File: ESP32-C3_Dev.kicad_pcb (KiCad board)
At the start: 2 copper layers, 30.7 x 37.2 mm, 58 parts, among them J1 Conn_01x09_Pin, J2 Conn_01x02_Pin, J3 Conn_01x09_Pin, J4 USB_C_Receptacle_USB2.0_16P, J5 Conn_01x03_Socket, J6 Conn_01x03_Socket, J7 Conn_01x04_Pin, SW1 SW_MEC_5G, SW2 SW_MEC_5G, U1 ESP32-C3-WROOM-02, U2 AMS1117-3.3, U3 MCP73831-2-OT, U4 TLV9002S, U5 OLED_SSD1306

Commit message: wip schematic
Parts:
- removed D7: 1N5819WS, Diode_SMD:D_SOD-323
- removed J2: Conn_01x02_Pin, TerminalBlock_Phoenix:TerminalBlock_Phoenix_MKDS-1-2-3.81_1x02_P3.81mm_Horizontal
- removed J3: Conn_01x09_Pin, Connector_PinHeader_2.54mm:PinHeader_1x09_P2.54mm_Vertical
- added C13: 4u7, Capacitor_SMD:C_0603_1608Metric, F.Cu at (190.3, 99.5)
- added D8: 1N5819WS, Diode_SMD:D_SOD-323, F.Cu at (202.9, 114.0)
- added J8: Conn_01x02_Pin, TerminalBlock_Phoenix:TerminalBlock_Phoenix_MKDS-1-2-3.81_1x02_P3.81mm_Horizontal, F.Cu at (195.3, 103.0)
- added Q1: Dual_NMOS_8205A, Package_TO_SOT_SMD:SOT-23-6, F.Cu at (203.4, 110.3)
- added R16: 10K, Resistor_SMD:R_0603_1608Metric, F.Cu at (190.3, 102.1)
- added R18: 10K, Resistor_SMD:R_0603_1608Metric, F.Cu at (190.3, 104.6)
- added R19: 10K, Resistor_SMD:R_0603_1608Metric, F.Cu at (190.3, 107.1)
- added R20: 100K, Resistor_SMD:R_0603_1608Metric, F.Cu at (190.3, 109.6)
- added R21: 100K, Resistor_SMD:R_0603_1608Metric, F.Cu at (190.3, 112.1)
- added R22: 10k, Resistor_SMD:R_0603_1608Metric, F.Cu at (209.9, 99.5)
- added R23: 10k, Resistor_SMD:R_0603_1608Metric, F.Cu at (209.9, 102.1)
- added U6: TP4056, Package_SO:SOIC-8-1EP_3.9x4.9mm_P1.27mm_EP2.41x3.3mm_ThermalVias, F.Cu at (196.6, 111.3)
- C6, C9: value 4u7 -> 100n
- D5: value LED -> LED Rot
- D6: value LED -> LED Blau
- R7: value 10K -> 100R
- R8: value 10K -> 1K
- U3: value MCP73831-2-OT -> DW01A; footprint Package_TO_SOT_SMD:SOT-23-5 -> Package_TO_SOT_SMD:SOT-23-6
- moved C10 8.80 mm to (179.8, 70.4)
- moved C11 8.80 mm to (179.8, 72.9)
- moved C12 8.80 mm to (179.8, 75.4)
- moved R10 8.80 mm to (179.8, 80.4)
- moved R11 8.80 mm to (179.8, 82.9)
- moved R12 8.80 mm to (183.8, 70.4)
- moved R13 8.80 mm to (183.8, 72.9)
- moved R14 8.80 mm to (183.8, 75.4)
- moved R15 8.80 mm to (183.8, 77.9)
- moved R17 8.80 mm to (183.8, 80.4)
- moved R9 8.80 mm to (179.8, 77.9)
- moved U4 8.80 mm to (181.5, 86.5)
- moved J1 7.36 mm to (118.5, 68.7)
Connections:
- C6 pad 1: +5V -> USB5V
- C9 pad 1: /Power Supply/battery+ -> Net-(U3-VCC)
- C9 pad 2: GND -> /Power Supply/battery-
- D2 pad 2: /Power Supply/USB5V -> USB5V
- D4 pad 1: /Power Supply/USB5V -> USB5V
- J1 pad 1: /Controller/GPIO4 -> unconnected-(J1-Pin_1-Pad1)
- J1 pad 2: /Controller/GPIO5 -> unconnected-(J1-Pin_2-Pad2)
- J1 pad 3: /Controller/GPIO6 -> unconnected-(J1-Pin_3-Pad3)
- J1 pad 4: /Controller/GPIO7 -> /Controller/GPIO0
- J1 pad 5: /Controller/GPIO8 -> /Controller/GPIO10
- J4 pad A4: /Power Supply/USB5V -> USB5V
- J4 pad A9: /Power Supply/USB5V -> USB5V
- J4 pad B4: /Power Supply/USB5V -> USB5V
- J4 pad B9: /Power Supply/USB5V -> USB5V
- R7 pad 1: +3.3V -> /Power Supply/battery+
- R7 pad 2: /Power Supply/charge_stat -> Net-(U3-VCC)
- R8 pad 1: Net-(U3-PROG) -> Net-(U3-CS)
- U1 pad 11: /Controller/GPIO20 -> /Controller/I2C_SDA
- U1 pad 12: /Controller/GPIO21 -> /Controller/I2C_SCL
- U1 pad 15: /Controller/GPIO3 -> /Controller/UBAT
- U1 pad 16: /Controller/GPIO2 -> /Controller/READY
- U1 pad 17: /Controller/GPIO1 -> /Controller/CHARGING
- U1 pad 3: /Controller/GPIO4 -> /Controller/PT100_1
- U1 pad 4: /Controller/GPIO5 -> /Controller/PT100_2
- U1 pad 5: /Controller/GPIO6 -> /Controller/SHDN1
- U1 pad 6: /Controller/GPIO7 -> /Controller/SHDN2
- U3 pad 1: /Power Supply/charge_stat -> Net-(Q1A-G)
- U3 pad 2: GND -> Net-(U3-CS)
- U3 pad 3: /Power Supply/battery+ -> Net-(Q1B-G)
- U3 pad 4: +5V -> unconnected-(U3-TD-Pad4)
- U3 pad 5: Net-(U3-PROG) -> Net-(U3-VCC)
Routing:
- net USB5V: track 0.00 -> 20.9 mm
- net /Power Supply/USB5V: track 20.9 -> 0.00 mm
- net +3.3V: track 79.2 -> 67.2 mm
- net /Controller/GPIO4: track 7.52 -> 0.00 mm
- net /Controller/GPIO5: track 6.99 -> 0.00 mm
- net /Controller/GPIO10: track 6.50 -> 0.00 mm
- net /Controller/GPIO3: track 6.45 -> 0.00 mm
- net /Controller/GPIO8: track 24.2 -> 17.9 mm
- net /Controller/GPIO9: track 39.9 -> 33.8 mm
- net /Controller/GPIO20: track 6.07 -> 0.00 mm
- net /Controller/GPIO2: track 6.02 -> 0.00 mm
- net /Controller/GPIO21: track 5.64 -> 0.00 mm
- net /Controller/GPIO1: track 5.59 -> 0.00 mm
- net /Controller/GPIO7: track 5.24 -> 0.00 mm
- net /Controller/GPIO0: track 5.16 -> 0.00 mm
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
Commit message: wip - schematic and layout
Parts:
- removed J1: Conn_01x09_Pin, Connector_PinHeader_2.54mm:PinHeader_1x09_P2.54mm_Vertical
- removed J7: Conn_01x04_Pin, Connector_PinHeader_2.54mm:PinHeader_1x04_P2.54mm_Vertical
- removed kibuzzard-679A56A9: G***, kibuzzard-679A56A9
- removed kibuzzard-679A56D4: G***, kibuzzard-679A56D4
- removed kibuzzard-679A5707: G***, kibuzzard-679A5707
- removed kibuzzard-679A573A: G***, kibuzzard-679A573A
- removed kibuzzard-679A5C81: G***, kibuzzard-679A5C81
- removed kibuzzard-679A5D01: G***, kibuzzard-679A5D01
- removed kibuzzard-679A5D22: G***, kibuzzard-679A5D22
- added C14: 100n, Capacitor_SMD:C_0603_1608Metric, F.Cu at (136.6, 85.5)
- added C15: 100n, Capacitor_SMD:C_0603_1608Metric, F.Cu at (154.5, 62.5)
- added C16: 100n, Capacitor_SMD:C_0603_1608Metric, F.Cu at (155.5, 68.0)
- added G***: LOGO, _PS_LIB_PCB:Faust_logo, B.Cu at (140.8, 69.0)
- added TP1: TestPoint, TestPoint:TestPoint_Pad_D1.5mm, F.Cu at (152.5, 60.5)
- added TP2: TestPoint, TestPoint:TestPoint_Pad_D1.5mm, F.Cu at (154.0, 72.0)
- added TP3: TestPoint, TestPoint:TestPoint_Pad_D1.5mm, F.Cu at (137.8, 94.6)
- added TP4: TestPoint, TestPoint:TestPoint_Pad_D1.5mm, F.Cu at (141.7, 87.6)
- added TP5: TestPoint, TestPoint:TestPoint_Pad_D1.5mm, F.Cu at (147.6, 93.8)
- added U7: XC6206P182MR, Package_TO_SOT_SMD:TSOT-23, F.Cu at (139.1, 85.5)
- added U8: BMP388, BMP388:PQFN50P200X200X80-10N, F.Cu at (154.5, 65.0)
- added kibuzzard-68E97F46: G***, kibuzzard-68E97F46, F.Cu at (131.1, 101.0)
- added kibuzzard-68E97F95: G***, kibuzzard-68E97F95, F.Cu at (150.8, 92.3)
- added kibuzzard-68E97FB6: G***, kibuzzard-68E97FB6, F.Cu at (153.5, 92.7)
- added kibuzzard-68E97FD1: G***, kibuzzard-68E97FD1, F.Cu at (147.5, 85.0)
- added kibuzzard-68E97FF2: G***, kibuzzard-68E97FF2, F.Cu at (135.0, 83.5)
- added kibuzzard-68E98035: G***, kibuzzard-68E98035, F.Cu at (143.5, 83.5)
- added kibuzzard-68E98065: G***, kibuzzard-68E98065, F.Cu at (128.5, 67.0)
- added kibuzzard-68E980D7: G***, kibuzzard-68E980D7, F.Cu at (140.5, 73.5)
- added kibuzzard-68E98136: G***, kibuzzard-68E98136, F.Cu at (138.0, 77.5)
- added kibuzzard-68E98140: G***, kibuzzard-68E98140, F.Cu at (143.5, 77.5)
- added kibuzzard-68E98172: G***, kibuzzard-68E98172, F.Cu at (128.0, 65.0)
- added kibuzzard-68E982C0: G***, kibuzzard-68E982C0, F.Cu at (154.5, 60.0)
- added kibuzzard-68E982C9: G***, kibuzzard-68E982C9, F.Cu at (156.0, 72.0)
- added kibuzzard-68E98378: G***, kibuzzard-68E98378, F.Cu at (155.4, 79.7)
- added kibuzzard-68E98378: G***, kibuzzard-68E98378, F.Cu at (125.9, 79.7)
- added kibuzzard-68E98378: G***, kibuzzard-68E98378, B.Cu at (155.5, 79.5)
- added kibuzzard-68E98378: G***, kibuzzard-68E98378, B.Cu at (126.0, 79.5)
- added kibuzzard-68E983D3: G***, kibuzzard-68E983D3, B.Cu at (129.5, 71.5)
- added kibuzzard-68E983DB: G***, kibuzzard-68E983DB, B.Cu at (152.0, 71.5)
- added kibuzzard-68E98408: G***, kibuzzard-68E98408, B.Cu at (140.5, 101.0)
- added kibuzzard-68E9848D: G***, kibuzzard-68E9848D, B.Cu at (140.8, 60.5)
- added kibuzzard-68E9858B: G***, kibuzzard-68E9858B, B.Cu at (152.5, 89.0)
- added kibuzzard-68E985AE: G***, kibuzzard-68E985AE, F.Cu at (154.5, 86.0)
- added kibuzzard-68E986B5: G***, kibuzzard-68E986B5, F.Cu at (141.9, 85.6)
- added kibuzzard-68E986EB: G***, kibuzzard-68E986EB, F.Cu at (137.0, 96.5)
- added kibuzzard-68E9870E: G***, kibuzzard-68E9870E, F.Cu at (147.6, 95.4)
- J8: footprint TerminalBlock_Phoenix:TerminalBlock_Phoenix_MKDS-1-2-3.81_1x02_P3.81mm_Horizontal -> Connector_PinHeader_2.00mm:PinHeader_1x02_P2.00mm_Vertical
- U5: moved to B.Cu
- moved U5 71.0 mm to (140.6, 87.0), turned to 180 degrees
- moved R23 66.4 mm to (152.6, 68.5)
- moved R22 64.5 mm to (152.6, 70.0)
- moved Q1 56.6 mm to (151.0, 89.0), turned to 180 degrees
- moved D8 51.9 mm to (155.1, 94.0), turned to -90 degrees
- moved R20 48.1 mm to (148.1, 86.5)
- moved R17 47.6 mm to (136.2, 79.7), turned to 90 degrees
- moved C11 46.9 mm to (133.8, 82.2), turned to 180 degrees
- moved R21 46.7 mm to (151.3, 86.5)
- moved U6 46.7 mm to (151.4, 99.5), turned to 90 degrees
- moved R11 46.3 mm to (133.8, 77.7)
- moved R9 46.0 mm to (133.8, 79.2)
- moved R10 46.0 mm to (133.8, 80.7), turned to 180 degrees
- moved J8 42.7 mm to (154.6, 90.0), turned to 180 degrees
- moved U4 41.2 mm to (140.6, 81.2)
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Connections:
- C10 pad 1: +3.3V -> +1.8V
- D6 pad 2: /Controller/GPIO8 -> Net-(D6-A)
- R11 pad 1: +3.3V -> +1.8V
- R13 pad 1: +3.3V -> +1.8V
- R14 pad 1: +3.3V -> +1.8V
- R22 pad 1: /Controller/I2C_SDA -> /Controller/I2C_SCL
- R23 pad 1: /Controller/I2C_SCL -> /Controller/I2C_SDA
- R6 pad 1: /Controller/GPIO8 -> Net-(D6-A)
- R6 pad 2: +3.3V -> /Controller/GPIO8
- R9 pad 1: +3.3V -> +1.8V
- U1 pad 11: /Controller/I2C_SDA -> /Controller/I2C_SCL
- U1 pad 12: /Controller/I2C_SCL -> /Controller/I2C_SDA
- U1 pad 3: /Controller/PT100_1 -> /Controller/PT100_2
- U1 pad 4: /Controller/PT100_2 -> /Controller/PT100_1
- U4 pad 10: +3.3V -> +1.8V
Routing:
- net GND: track 2.92 -> 63.2 mm, vias 64 -> 24
- net +3.3V: track 67.2 -> 118.3 mm, vias 4 -> 2
- net /Controller/CHARGING: track 0.00 -> 45.2 mm, vias 0 -> 2
- net /Controller/READY: track 0.00 -> 41.5 mm, vias 0 -> 2
- net +1.8V: track 0.00 -> 35.1 mm, vias 0 -> 3
- net /Controller/SHDN2: track 0.00 -> 29.3 mm, vias 0 -> 2
- net /Controller/PT100_2: track 0.21 -> 29.2 mm, vias 0 -> 2
- net /Controller/UBAT: track 0.00 -> 27.6 mm, vias 0 -> 2
- net /Controller/SHDN1: track 0.00 -> 25.0 mm, vias 0 -> 2
- net /Power Supply/battery+: track 0.00 -> 24.9 mm
- net /Controller/I2C_SCL: track 0.00 -> 22.8 mm, vias 0 -> 2
- net /Controller/I2C_SDA: track 0.00 -> 21.9 mm
- net /Controller/PT100_1: track 0.54 -> 21.4 mm, vias 0 -> 2
- net /Power Supply/battery-: track 0.00 -> 14.8 mm
- net Net-(J6-Pin_2): track 0.00 -> 14.8 mm
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- added copper zone on F.Cu, net +3.3V
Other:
- board size 30.7 x 37.2 mm -> 32.7 x 47.2 mm
- board text added: "JLCJLCJLCJLC"

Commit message: wip
lcsc part numbers
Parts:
- removed U7: XC6206P182MR, Package_TO_SOT_SMD:TSOT-23
- removed kibuzzard-68E97F95: G***, kibuzzard-68E97F95
- removed kibuzzard-68E97FB6: G***, kibuzzard-68E97FB6
- removed kibuzzard-68E98136: G***, kibuzzard-68E98136
- removed kibuzzard-68E98140: G***, kibuzzard-68E98140
- removed kibuzzard-68E982C0: G***, kibuzzard-68E982C0
- removed kibuzzard-68E982C9: G***, kibuzzard-68E982C9
- removed the kibuzzard-68E98378 at (155.5, 79.5)
- removed the kibuzzard-68E98378 at (126.0, 79.5)
- added R24: 3K3, Resistor_SMD:R_0603_1608Metric, F.Cu at (148.3, 83.9)
- added R25: 1M, Resistor_SMD:R_0603_1608Metric, F.Cu at (145.3, 79.2)
- added R26: 3K3, Resistor_SMD:R_0603_1608Metric, F.Cu at (148.3, 77.7)
- added R27: 3K3, Resistor_SMD:R_0603_1608Metric, F.Cu at (133.3, 83.9)
- added R28: 3K3, Resistor_SMD:R_0603_1608Metric, F.Cu at (133.3, 77.7)
- added R29: 1M, Resistor_SMD:R_0603_1608Metric, F.Cu at (136.3, 82.2)
- added U9: XC6220B181MR, Package_TO_SOT_SMD:SOT-23-5, F.Cu at (139.1, 85.5)
- added kibuzzard-68EE7166: G***, kibuzzard-68EE7166, F.Cu at (126.0, 65.0)
- added kibuzzard-68EE716B: G***, kibuzzard-68EE716B, F.Cu at (128.0, 67.0)
- added kibuzzard-68EE7185: G***, kibuzzard-68EE7185, F.Cu at (138.0, 77.0)
- added kibuzzard-68EE718D: G***, kibuzzard-68EE718D, F.Cu at (143.5, 77.0)
- added kibuzzard-68EE71B1: G***, kibuzzard-68EE71B1, F.Cu at (151.5, 91.5)
- added kibuzzard-68EE71C0: G***, kibuzzard-68EE71C0, F.Cu at (153.5, 94.0)
- added kibuzzard-68EE7E42: G***, kibuzzard-68EE7E42, B.Cu at (155.5, 79.5)
- added kibuzzard-68EE7E4D: G***, kibuzzard-68EE7E4D, B.Cu at (126.0, 79.5)
- C7, SW1, kibuzzard-68E97F46: moved to B.Cu
- R12, R17: value 33K -> 1M
- moved kibuzzard-68E97F46 33.5 mm to (141.3, 69.0), turned to 180 degrees
- moved SW1 30.2 mm to (140.8, 71.5), turned to 180 degrees
- moved kibuzzard-68E98172 26.4 mm to (153.5, 72.0)
- moved C7 25.7 mm to (136.5, 71.5), turned to -90 degrees
- moved TP1 24.9 mm to (128.0, 65.0)
- moved TP2 24.8 mm to (129.8, 66.4)
- moved G*** 9.51 mm to (131.5, 67.0), turned to -90 degrees
- moved kibuzzard-68E98065 5.70 mm to (127.0, 72.5)
- moved R15 4.55 mm to (146.8, 77.7), turned to 90 degrees
- moved kibuzzard-68E97FF2 4.53 mm to (139.5, 83.0)
- moved kibuzzard-68E97FD1 3.50 mm to (151.0, 85.0)
- moved C12 3.30 mm to (146.8, 83.9), turned to -90 degrees
- moved R10 3.16 mm to (134.8, 77.7), turned to 90 degrees
- moved R14 2.54 mm to (148.0, 81.7)
- moved R12 2.52 mm to (145.3, 82.2), turned to -90 degrees
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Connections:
- J5 pad 1: Net-(J5-Pin_1) -> GND
- J5 pad 3: GND -> Net-(J5-Pin_3)
- J6 pad 1: Net-(J6-Pin_1) -> GND
- J6 pad 3: GND -> Net-(J6-Pin_3)
- R10 pad 1: Net-(U4A--) -> Net-(R10-Pad1)
- R11 pad 1: +1.8V -> Net-(R10-Pad1)
- R11 pad 2: Net-(J5-Pin_1) -> Net-(U4A--)
- R12 pad 1: Net-(U4B--) -> Net-(U4B-+)
- R12 pad 2: /Controller/PT100_2 -> GND
- R13 pad 1: +1.8V -> Net-(R13-Pad1)
- R13 pad 2: Net-(J6-Pin_1) -> Net-(U4B--)
- R14 pad 1: +1.8V -> Net-(J6-Pin_2)
- R14 pad 2: Net-(U4B--) -> Net-(U4B-+)
- R15 pad 1: Net-(U4B--) -> Net-(R13-Pad1)
- R9 pad 1: +1.8V -> Net-(J5-Pin_2)
- R9 pad 2: Net-(U4A--) -> Net-(U4A-+)
- TP1 pad 1: /Controller/GPIO0 -> Net-(U1-IO4)
- TP2 pad 1: /Controller/GPIO10 -> Net-(U1-IO5)
- U1 pad 10: /Controller/GPIO10 -> /Controller/CHARGING
- U1 pad 16: /Controller/READY -> /Controller/PT100_2
- U1 pad 17: /Controller/CHARGING -> /Controller/PT100_1
- U1 pad 18: /Controller/GPIO0 -> /Controller/READY
- U1 pad 3: /Controller/PT100_2 -> Net-(U1-IO4)
- U1 pad 4: /Controller/PT100_1 -> Net-(U1-IO5)
- U4 pad 3: Net-(J5-Pin_2) -> Net-(U4A-+)
- U4 pad 7: Net-(J6-Pin_2) -> Net-(U4B-+)
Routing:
- net /Controller/GPIO9: track 40.9 -> 7.34 mm, vias 2 -> 1
- net /Controller/PT100_1: track 21.4 -> 34.7 mm
- net GND: track 63.2 -> 50.5 mm, vias 24 -> 65
- net +1.8V: track 35.1 -> 47.0 mm
- net /Controller/SHDN1: track 25.0 -> 35.6 mm, vias 2 -> 3
- net /Controller/CHARGING: track 45.2 -> 35.9 mm
- net /Controller/PT100_2: track 29.2 -> 21.7 mm
- net Net-(J6-Pin_1): track 7.25 -> 0.00 mm
- net Net-(J5-Pin_1): track 7.19 -> 0.00 mm
- net Net-(J6-Pin_2): track 14.8 -> 8.11 mm
- net Net-(U1-IO4): track 0.00 -> 5.79 mm
- net Net-(J5-Pin_3): track 0.00 -> 5.27 mm
- net Net-(J6-Pin_3): track 0.00 -> 5.27 mm
- net /Controller/GPIO10: track 4.61 -> 0.00 mm
- net Net-(U4A-+): track 0.00 -> 4.47 mm
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
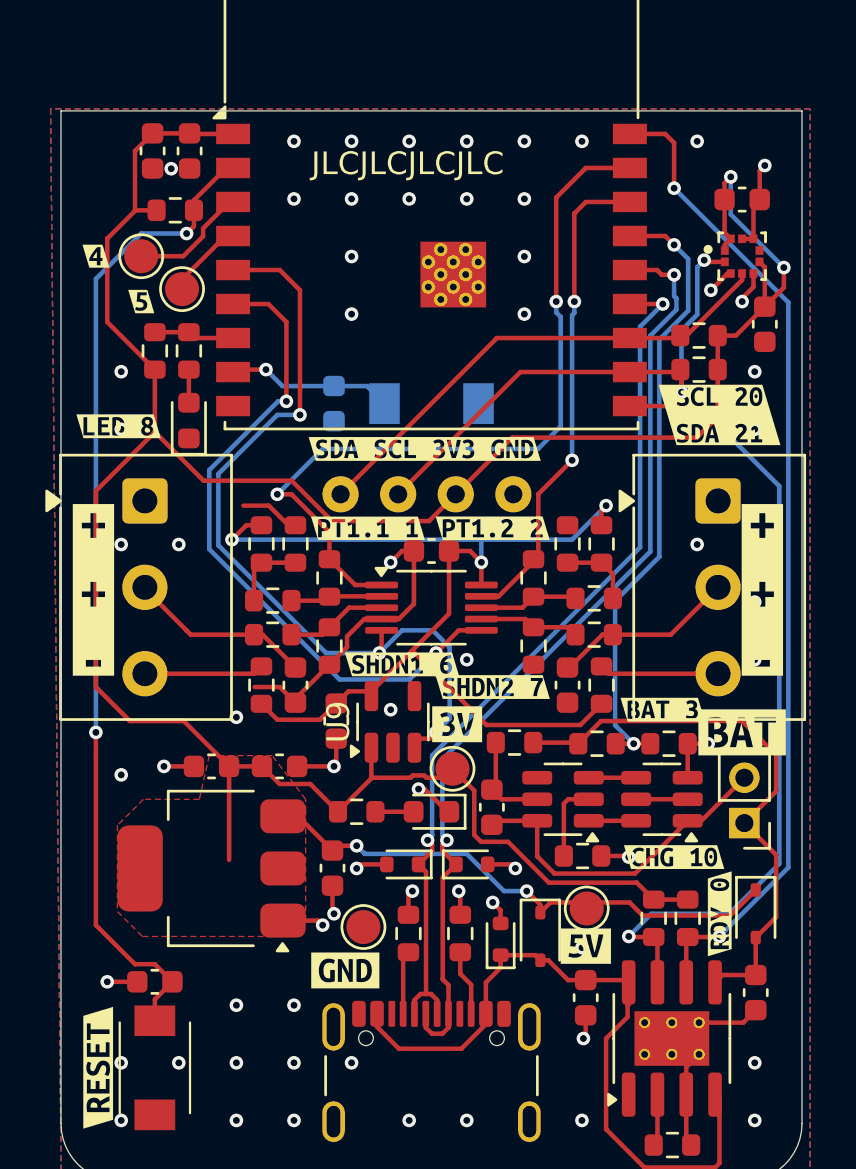
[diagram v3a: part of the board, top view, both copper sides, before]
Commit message: level shift for op en added
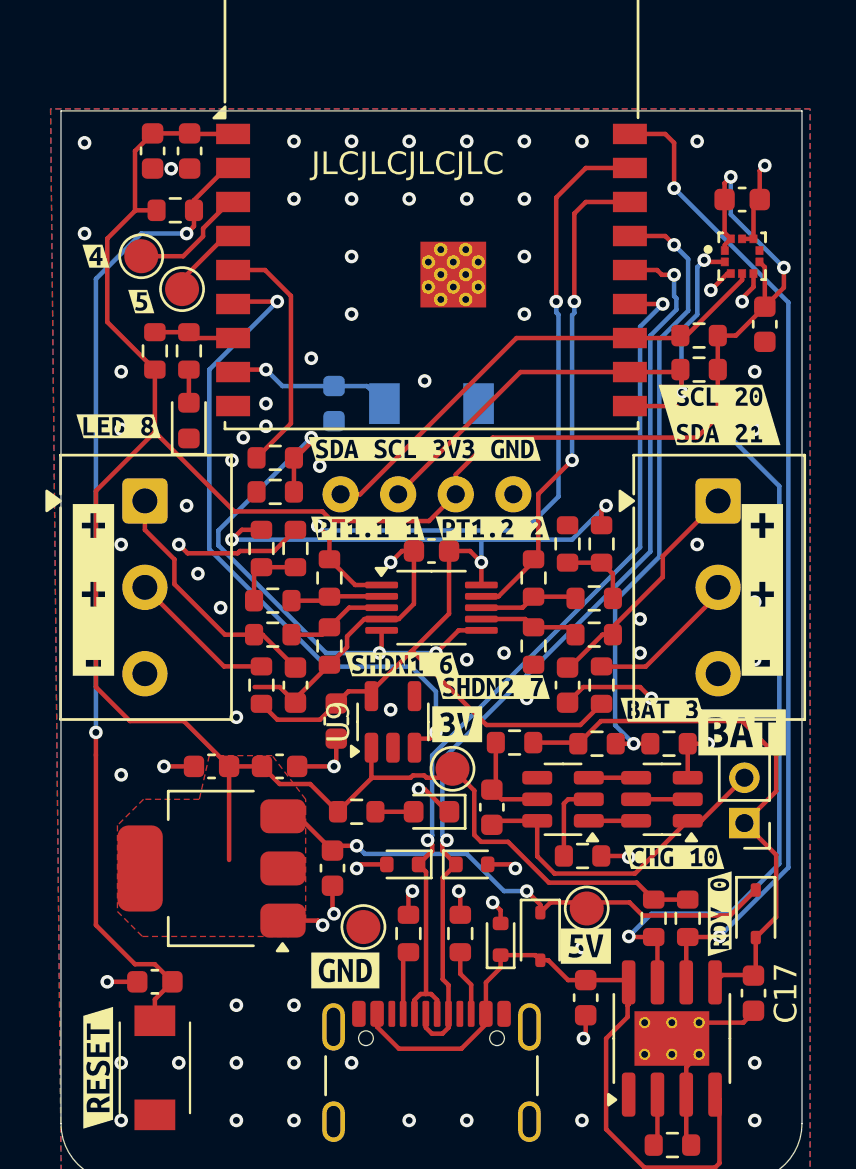
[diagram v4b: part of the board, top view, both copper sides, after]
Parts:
- removed C13: 4u7, Capacitor_SMD:C_0603_1608Metric
- added C17: 10u 10V, Capacitor_SMD:C_0603_1608Metric, F.Cu at (155.0, 97.5)
- added R30: 10k, Resistor_SMD:R_0603_1608Metric, F.Cu at (133.9, 73.9)
- added R31: 10k, Resistor_SMD:R_0603_1608Metric, F.Cu at (133.9, 75.4)
- C1, C2, C4: value 10u 25V -> 10u 10V
- R10, R15: value 91R -> 91R .1%
- R11, R13, R14, R9: value 10K -> 10K .1%
- R12, R17, R25, R29: value 1M -> 1M .1%
- R24, R26, R27, R28: value 3K3 -> 3K3 .1%
- moved R10 0.20 mm to (134.8, 77.9)
- moved R28 0.20 mm to (133.3, 77.9)
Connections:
- C11 pad 1: Net-(J5-Pin_2) -> Net-(J5-Pin_1)
- C12 pad 1: Net-(J6-Pin_2) -> Net-(J6-Pin_1)
- J5 pad 1: GND -> Net-(J5-Pin_1)
- J5 pad 3: Net-(J5-Pin_3) -> GND
- J6 pad 1: GND -> Net-(J6-Pin_1)
- J6 pad 3: Net-(J6-Pin_3) -> GND
- R14 pad 1: Net-(J6-Pin_2) -> Net-(J6-Pin_1)
- R24 pad 2: Net-(J6-Pin_3) -> Net-(J6-Pin_2)
- R27 pad 2: Net-(J5-Pin_3) -> Net-(J5-Pin_2)
- R9 pad 1: Net-(J5-Pin_2) -> Net-(J5-Pin_1)
- U1 pad 5: /Controller/SHDN1 -> Net-(U1-IO6)
- U1 pad 6: /Controller/SHDN2 -> /Controller/SHDNLDO
- U4 pad 6: /Controller/SHDN2 -> /Controller/SHDN1
- U9 pad 3: /Controller/SHDN1 -> /Controller/SHDNLDO
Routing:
- net /Controller/SHDNLDO: track 0.00 -> 29.6 mm, vias 0 -> 2
- net /Controller/SHDN2: track 29.6 -> 0.00 mm, vias 2 -> 0
- net /Controller/SHDN1: track 35.6 -> 24.3 mm
- net Net-(J5-Pin_1): track 0.00 -> 11.1 mm
- net Net-(U1-IO6): track 0.00 -> 10.8 mm
- net Net-(J6-Pin_1): track 0.00 -> 10.4 mm
- net GND: track 50.5 -> 58.0 mm, vias 65 -> 82
- net Net-(J5-Pin_3): track 5.27 -> 0.00 mm
- net Net-(J6-Pin_3): track 5.27 -> 0.00 mm
- net /Controller/PT100_1: track 34.7 -> 32.8 mm
- net Net-(J5-Pin_2): track 8.05 -> 6.58 mm
- net Net-(J6-Pin_2): track 8.11 -> 6.77 mm
- net +3.3V: track 117.8 -> 118.3 mm

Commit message: wip
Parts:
- moved kibuzzard-68E98378 0.39 mm to (155.7, 79.5)
- moved kibuzzard-68EE7E42 0.21 mm to (155.7, 79.5)
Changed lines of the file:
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@@
 	(footprint "kibuzzard-68E98378"
 		(layer "F.Cu")
-		(at 155.391151 79.715915)
+		(at 155.71 79.5)
 		(descr "Generated with KiBuzzard")
 		(tags "kb_params=eyJBbGlnbm1lbnRDaG9pY2UiOiAiQ2VudGVyIiwgIkNhcExlZnRDaG9pY2UiOiAiWyIsICJDYXBSaWdodENob2ljZSI6ICJdIiwgIkZvbnRDb21ib0JveCI6ICJVYnVudHVNb25vLUIiLCAiSGVpZ2h0Q3RybCI6IDEuNSwgIkxheWVyQ29tYm9Cb3giOiAiRi5TaWxrUyIsICJMaW5lU3BhY2luZ0N0cmwiOiAxLjUsICJNdWx0aUxpbmVUZXh0IjogIitcclxuK1xyXG4tIiwgIlBhZGRpbmdCb3R0b21DdHJsIjogMi4wLCAiUGFkZGluZ0xlZnRDdHJsIjogMi4wLCAiUGFkZGluZ1JpZ2h0Q3RybCI6IDIuMCwgIlBhZGRpbmdUb3BDdHJsIjogMi4wLCAiV2lkdGhDdHJsIjogMC4wLCAiYWR2YW5jZWRDaGVja2JveCI6IGZhbHNlLCAiaW5saW5lRm9ybWF0VGV4dGJveCI6IGZhbHNlLCAibGluZW92ZXJTdHlsZUNob2ljZSI6ICJTcXVhcmUiLCAibGluZW92ZXJUaGlja25lc3NDdHJsIjogMX0=")
@@
 	(footprint "kibuzzard-68EE7E42"
 		(layer "B.Cu")
-		(at 155.5 79.5 180)
+		(at 155.71 79.5 180)
 		(descr "Generated with KiBuzzard")
 		(tags "kb_params=eyJBbGlnbm1lbnRDaG9pY2UiOiAiQ2VudGVyIiwgIkNhcExlZnRDaG9pY2UiOiAiWyIsICJDYXBSaWdodENob2ljZSI6ICJdIiwgIkZvbnRDb21ib0JveCI6ICJVYnVudHVNb25vLUIiLCAiSGVpZ2h0Q3RybCI6IDEuNSwgIkxheWVyQ29tYm9Cb3giOiAiRi5TaWxrUyIsICJMaW5lU3BhY2luZ0N0cmwiOiAxLjUsICJNdWx0aUxpbmVUZXh0IjogIi1cclxuK1xyXG4rIiwgIlBhZGRpbmdCb3R0b21DdHJsIjogMi4wLCAiUGFkZGluZ0xlZnRDdHJsIjogMi4wLCAiUGFkZGluZ1JpZ2h0Q3RybCI6IDIuMCwgIlBhZGRpbmdUb3BDdHJsIjogMi4wLCAiV2lkdGhDdHJsIjogMC4wLCAiYWR2YW5jZWRDaGVja2JveCI6IGZhbHNlLCAiaW5saW5lRm9ybWF0VGV4dGJveCI6IGZhbHNlLCAibGluZW92ZXJTdHlsZUNob2ljZSI6ICJTcXVhcmUiLCAibGluZW92ZXJUaGlja25lc3NDdHJsIjogMX0=")
